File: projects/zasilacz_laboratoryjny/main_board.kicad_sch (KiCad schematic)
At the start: 109 parts, among them J1 AX301x2, J10 PWRL−, J101 INSULATED FERRULE, J102 INSULATED FERRULE, J103 OFF_BOARD, J104 OFF_BOARD, J105 OFF_BOARD, J106 OFF_BOARD, J107 OFF_BOARD, J108 OFF_BOARD, J109 OFF_BOARD, J11 VSET1, J110 OFF_BOARD, J111 OFF_BOARD, J112 OFF_BOARD, J113 OFF_BOARD, J114 OFF_BOARD, J115 OFF_BOARD, J116 OFF_BOARD, J117 OFF_BOARD, J118 OFF_BOARD, J119 OFF_BOARD, J12 VSET2, J120 OFF_BOARD, J121 OFF_BOARD, J122 OFF_BOARD, J123 OFF_BOARD, J124 OFF_BOARD, J125 INSULATED FERRULE, J126 INSULATED FERRULE, J127 BARREL JACK 2,1/5,5, J128 BANANA JACK 4mm, J129 BANANA JACK 4mm, J13 OCPL+, J14 OCPL−, J15 VDOL+, J16 VDOL−, J17 OCP1, J18 OCP2, J19 OCP3, J2 AX301x2, J20 OCP4, J21 OCP5, J22 OCP6, J23 OCP7, J24 OCP8, J25 FAN+, J26 FAN−, J5 VMPROBE, J6 VMPWR, J7 VMGND, J8 OCP0, J9 PWRL+, P1 10kΩ, SW1 SW_SP8T, SW2 ROCKER SWITCH, T1 BC557, T2 BC557, T3 BC547, T4 BC547, T5 BC557, T6 BC557, T7 BS170, T8 BC547, U1 DB207, U2 LM317, Y1 3V

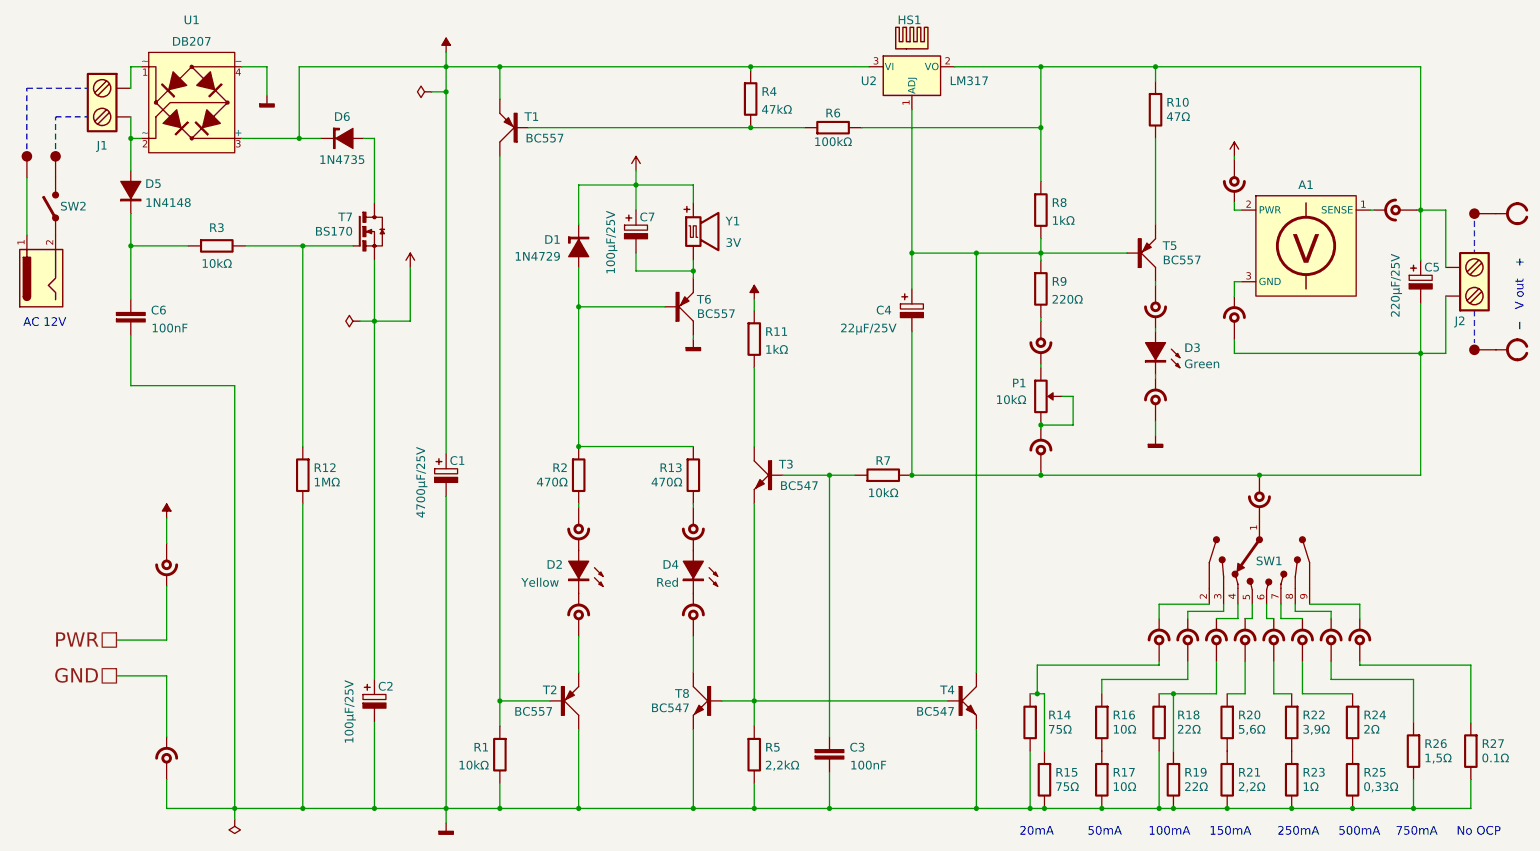
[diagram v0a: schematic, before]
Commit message: project updates (kicad upgrade related?)
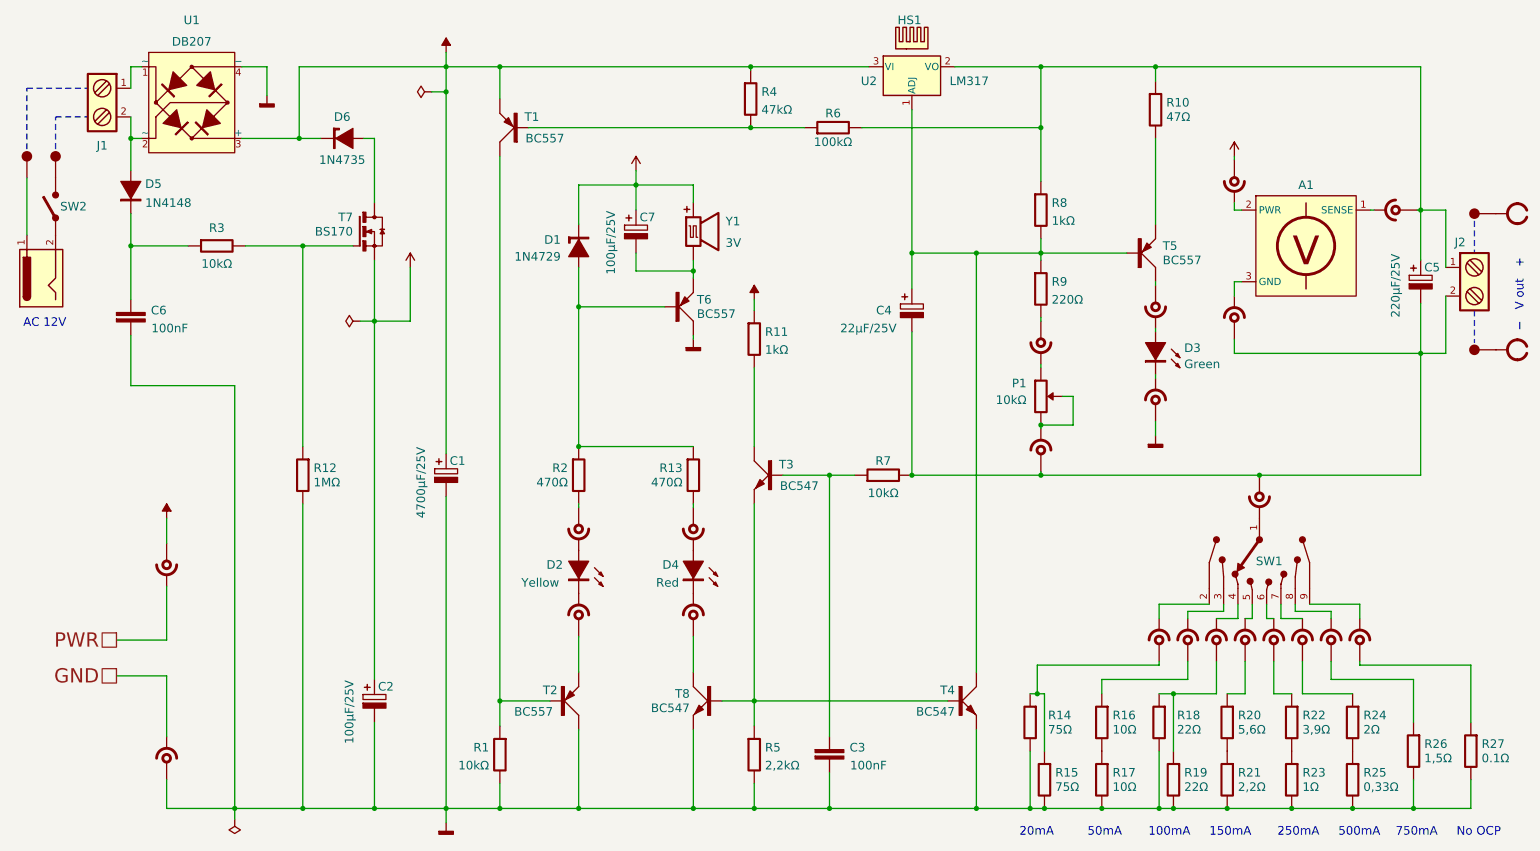
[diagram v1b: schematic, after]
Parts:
- A1: symbol *Custom_Generic:Voltmeter_digital -> Custom_Generic:Voltmeter_digital
- J1, J2: symbol *Custom_Generic:Terminal_Block_x2 -> Custom_Generic:Terminal_Block_x2
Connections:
- net at C5.2 (+), J5.1 (Pin_1), R10.1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: now also J2.1 (Pin_1); no longer J2.2 (Pin_2)
- net at C4.1 (-), C5.1 (-), J12.1 (Pin_1)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: now also J2.2 (Pin_2); no longer J2.1 (Pin_1)
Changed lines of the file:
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@@
     )
   )
-  (symbol (lib_id "*Custom_Generic:Voltmeter_digital") (at 243.84 59.055 0) (unit 1)
+  (symbol (lib_id "Custom_Generic:Voltmeter_digital") (at 243.84 59.055 0) (unit 1)
     (in_bom yes) (on_board no) (dnp no)
     (property "Reference" "A1" (at 243.84 48.26 0)
@@
     )
   )
-  (symbol (lib_id "*Custom_Generic:Terminal_Block_x2") (at 30.48 33.655 0) (mirror y) (unit 1)
+  (symbol (lib_id "Custom_Generic:Terminal_Block_x2") (at 30.48 33.655 0) (mirror y) (unit 1)
     (in_bom yes) (on_board yes) (dnp no)
     (property "Reference" "J1" (at 30.48 41.275 0)
@@
     )
   )
-  (symbol (lib_name "Terminal_Block_x2_1") (lib_id "*Custom_Generic:Terminal_Block_x2") (at 273.685 65.405 0) (mirror x) (unit 1)
-    (in_bom yes) (on_board yes) (dnp no)
-    (property "Reference" "J2" (at 271.145 72.39 0)
+  (symbol (lib_id "Custom_Generic:Terminal_Block_x2") (at 273.685 65.405 0) (unit 1)
+    (in_bom yes) (on_board yes) (dnp no)
+    (property "Reference" "J2" (at 271.145 58.42 0)
       (effects (font (size 1.524 1.524)))
     )
-    (property "Value" "AX301x2" (at 276.86 62.8651 0)
+    (property "Value" "AX301x2" (at 276.86 67.9449 0)
       (effects (font (size 1.524 1.524)) hide)
     )
